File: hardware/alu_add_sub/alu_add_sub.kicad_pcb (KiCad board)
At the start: 4 copper layers, 99 x 84 mm, 162 parts, among them J1 Conn_02x22_Odd_Even, Q1 IRLML6244, Q10 IRLML6244, Q11 IRLML6244, Q12 IRLML6244, Q13 IRLML6244, Q14 IRLML6244, Q15 IRLML6244, Q16 IRLML6244, Q17 IRLML6244, Q18 IRLML6244, Q19 IRLML6244, Q2 IRLML6244, Q20 IRLML6244, Q21 IRLML6244, Q22 IRLML6244, Q23 IRLML6244, Q24 IRLML6244, Q25 IRLML6244, Q26 IRLML6244, Q27 IRLML6244, Q28 IRLML6244, Q3 IRLML6244, Q4 IRLML6244, Q5 IRLML6244, Q6 IRLML6244, Q7 IRLML6244, Q8 IRLML6244, Q9 IRLML6244, U1 74HC00, U10 74HC00, U11 74HC00, U12 74HC00, U13 74HC00, U14 74HC00, U15 74HC00, U16 74HC00, U17 74HC00, U18 74HC00, U19 74HC00, U2 74HC00, U20 74HC00, U21 74HC00, U22 74HC00, U23 74HC00, U24 74HC00, U25 74HC00, U26 74HC00, U27 74HC00, U28 74HC00, U29 74HC00, U3 74HC00, U30 74HC00, U31 74HC00, U32 74HC00, U33 74HC00, U34 74HC00, U35 74HC00, U4 74HC00, U5 74HC00, U6 74HC00, U7 74HC00, U8 74HC00, U9 74HC00

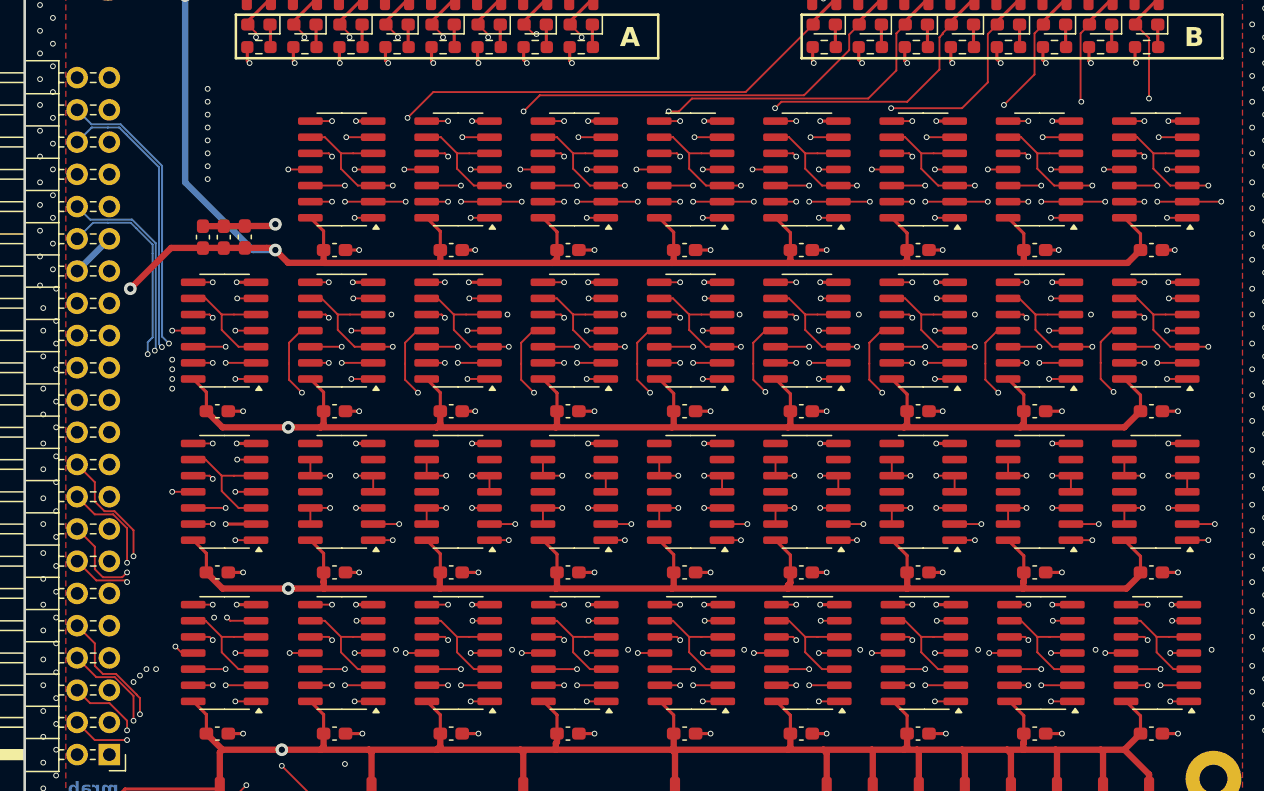
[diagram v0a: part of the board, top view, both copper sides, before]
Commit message: finalized PCB for ordering (LCSC parts, silkscreen, etc)
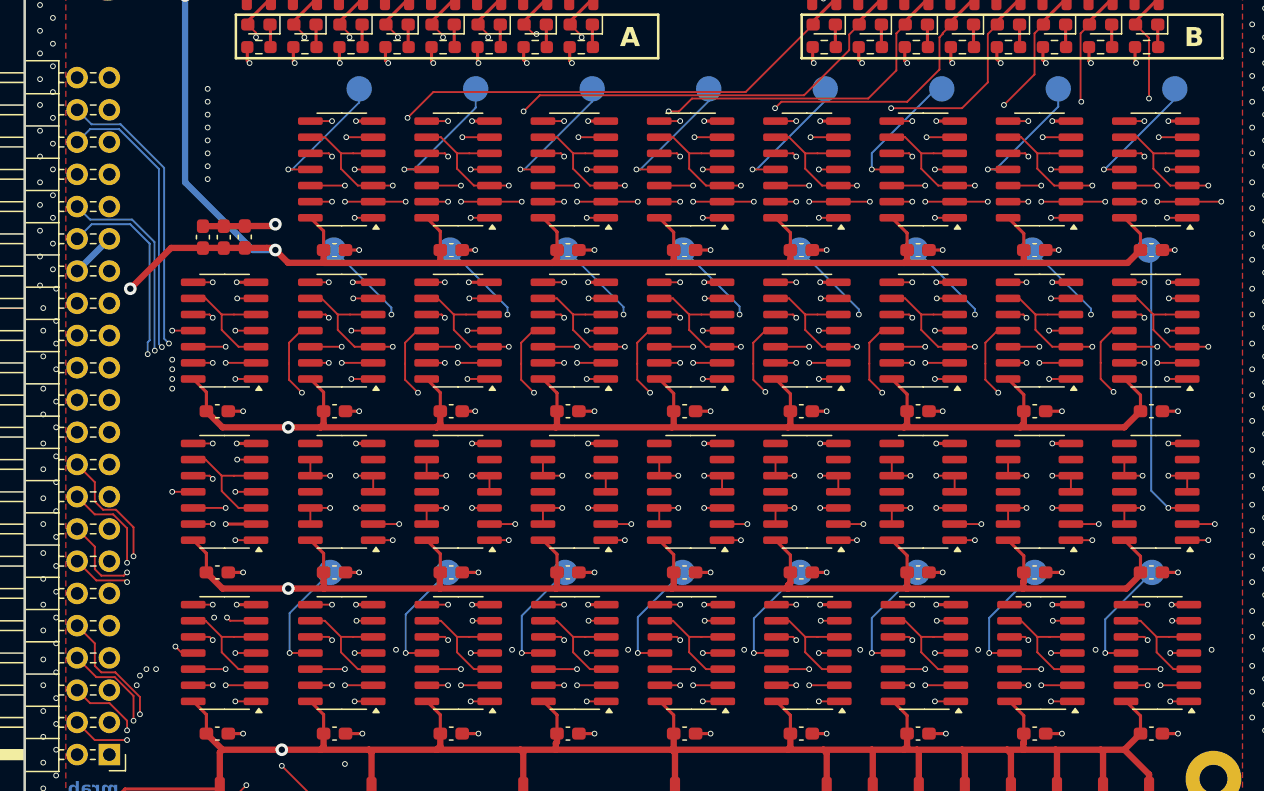
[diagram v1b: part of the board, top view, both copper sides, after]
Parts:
- added TP1: TestPoint, TestPoint:TestPoint_Pad_D2.0mm, B.Cu at (125.0, 109.2)
- added TP10: TestPoint, TestPoint:TestPoint_Pad_D2.0mm, B.Cu at (134.4, 83.8)
- added TP11: TestPoint, TestPoint:TestPoint_Pad_D2.0mm, B.Cu at (143.6, 83.8)
- added TP12: TestPoint, TestPoint:TestPoint_Pad_D2.0mm, B.Cu at (152.8, 83.8)
- added TP13: TestPoint, TestPoint:TestPoint_Pad_D2.0mm, B.Cu at (161.9, 83.8)
- added TP14: TestPoint, TestPoint:TestPoint_Pad_D2.0mm, B.Cu at (171.1, 83.8)
- added TP15: TestPoint, TestPoint:TestPoint_Pad_D2.0mm, B.Cu at (180.3, 83.8)
- added TP16: TestPoint, TestPoint:TestPoint_Pad_D2.0mm, B.Cu at (189.5, 83.8)
- added TP17: TestPoint, TestPoint:TestPoint_Pad_D2.0mm, B.Cu at (127.3, 71.1)
- added TP18: TestPoint, TestPoint:TestPoint_Pad_D2.0mm, B.Cu at (136.4, 71.1)
- added TP19: TestPoint, TestPoint:TestPoint_Pad_D2.0mm, B.Cu at (145.6, 71.1)
- added TP2: TestPoint, TestPoint:TestPoint_Pad_D2.0mm, B.Cu at (134.2, 109.2)
- added TP20: TestPoint, TestPoint:TestPoint_Pad_D2.0mm, B.Cu at (154.8, 71.1)
- added TP21: TestPoint, TestPoint:TestPoint_Pad_D2.0mm, B.Cu at (164.0, 71.1)
- added TP22: TestPoint, TestPoint:TestPoint_Pad_D2.0mm, B.Cu at (173.2, 71.1)
- added TP23: TestPoint, TestPoint:TestPoint_Pad_D2.0mm, B.Cu at (182.3, 71.1)
- added TP24: TestPoint, TestPoint:TestPoint_Pad_D2.0mm, B.Cu at (191.5, 71.1)
- added TP3: TestPoint, TestPoint:TestPoint_Pad_D2.0mm, B.Cu at (143.5, 109.2)
- added TP4: TestPoint, TestPoint:TestPoint_Pad_D2.0mm, B.Cu at (152.7, 109.2)
- added TP5: TestPoint, TestPoint:TestPoint_Pad_D2.0mm, B.Cu at (162.0, 109.2)
- added TP6: TestPoint, TestPoint:TestPoint_Pad_D2.0mm, B.Cu at (171.2, 109.2)
- added TP7: TestPoint, TestPoint:TestPoint_Pad_D2.0mm, B.Cu at (180.5, 109.2)
- added TP8: TestPoint, TestPoint:TestPoint_Pad_D2.0mm, B.Cu at (189.7, 109.2)
- added TP9: TestPoint, TestPoint:TestPoint_Pad_D2.0mm, B.Cu at (125.2, 83.8)
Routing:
- net Net-(TP16-Pad1): track 99.2 -> 120.2 mm
- net Net-(TP18-Pad1): track 24.5 -> 33.6 mm
- net Net-(TP23-Pad1): track 24.2 -> 33.2 mm
- net Net-(TP21-Pad1): track 24.4 -> 33.4 mm
- net Net-(TP22-Pad1): track 24.1 -> 33.0 mm
- net Net-(TP20-Pad1): track 24.6 -> 33.5 mm
- net Net-(TP19-Pad1): track 24.4 -> 33.3 mm
- net Net-(TP17-Pad1): track 24.3 -> 33.1 mm
- net Net-(TP24-Pad1): track 24.5 -> 33.2 mm
- net Net-(TP8-Pad1): track 56.6 -> 64.5 mm
- net Net-(TP5-Pad1): track 56.6 -> 64.5 mm
- net Net-(TP6-Pad1): track 56.6 -> 64.5 mm
- net Net-(TP7-Pad1): track 56.6 -> 64.5 mm
- net Net-(TP4-Pad1): track 56.6 -> 64.4 mm
- net Net-(TP3-Pad1): track 56.6 -> 64.4 mm
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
